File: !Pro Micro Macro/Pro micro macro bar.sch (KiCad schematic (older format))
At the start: 19 parts, among them U1 ProMicro

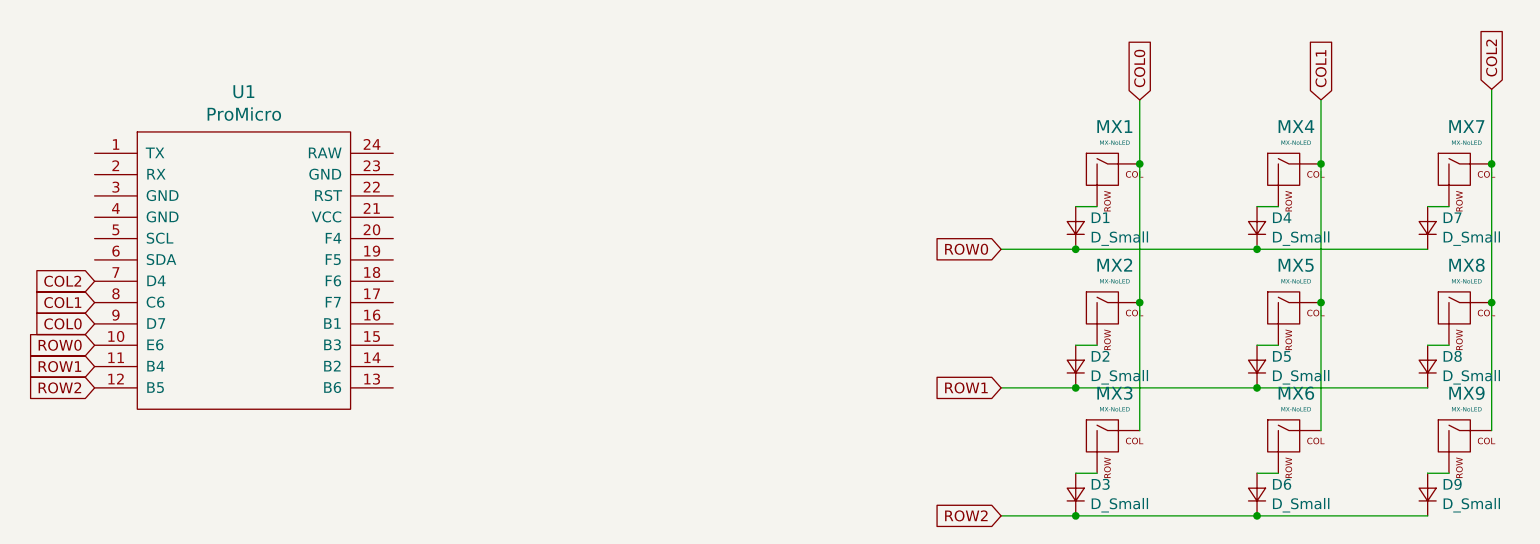
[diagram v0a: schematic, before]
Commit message: Redesigned pro micro
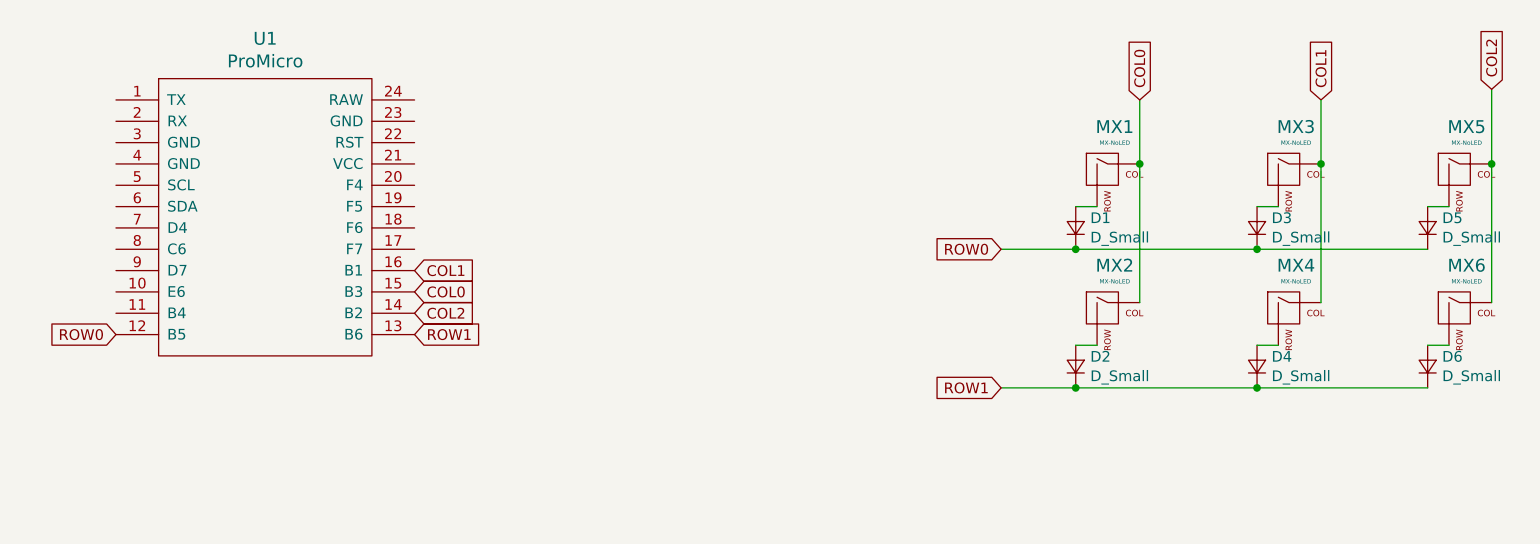
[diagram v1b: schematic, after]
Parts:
- removed D3, D6, D9: D_Small, Diode_THT:D_A-405_P10.16mm_Horizontal, symbol Device:D_Small
- removed MX3, MX6, MX9: MX-NoLED, Bases github:MX-1U-NoLED, symbol MX_Alps_Hybrid:MX-NoLED
- D1, D2: footprint Diode_THT:D_A-405_P10.16mm_Horizontal -> random-keyboard-parts:D_SOD-123-Pretty
- D3: renamed from D4; footprint Diode_THT:D_A-405_P10.16mm_Horizontal -> random-keyboard-parts:D_SOD-123-Pretty
- D4: renamed from D5; footprint Diode_THT:D_A-405_P10.16mm_Horizontal -> random-keyboard-parts:D_SOD-123-Pretty
- D5: renamed from D7; footprint Diode_THT:D_A-405_P10.16mm_Horizontal -> random-keyboard-parts:D_SOD-123-Pretty
- D6: renamed from D8; footprint Diode_THT:D_A-405_P10.16mm_Horizontal -> random-keyboard-parts:D_SOD-123-Pretty
- MX1, MX2: footprint Bases github:MX-1U-NoLED -> ! MX bases:MXOnly-1U-Hotswap
- MX3: renamed from MX4; footprint Bases github:MX-1U-NoLED -> ! MX bases:MXOnly-1U-Hotswap
- MX4: renamed from MX5; footprint Bases github:MX-1U-NoLED -> ! MX bases:MXOnly-1U-Hotswap
- MX5: renamed from MX7; footprint Bases github:MX-1U-NoLED -> ! MX bases:MXOnly-1U-Hotswap
- MX6: renamed from MX8; footprint Bases github:MX-1U-NoLED -> ! MX bases:MXOnly-1U-Hotswap
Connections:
- net ROW2 is gone; now on net ROW0: U1.12 (B5)
- net COL0: now also U1.15 (B3); no longer U1.9 (D7)
- net COL1: now also U1.16 (B1); no longer U1.8 (C6)
- net COL2: now also U1.14 (B2); no longer U1.7 (D4)
- net ROW0: no longer U1.10 (E6)
- net ROW1: now also U1.13 (B6); no longer U1.11 (B4)
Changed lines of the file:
@@
 $EndDescr
-$Comp
-L promicro:ProMicro U1
-U 1 1 5DA52A12
-P 3000 3350
-F 0 "U1" H 3000 4387 60  0000 C CNN
-F 1 "ProMicro" H 3000 4281 60  0000 C CNN
-F 2 "promicro:ProMicro" H 3100 2300 60  0001 C CNN
-F 3 "" H 3100 2300 60  0000 C CNN
-	1    3000 3350
-	1    0    0    -1
-$EndComp
 $Comp
 L MX_Alps_Hybrid:MX-NoLED MX1
@@
 F 0 "MX1" H 7083 2923 60  0000 C CNN
 F 1 "MX-NoLED" H 7083 2849 20  0000 C CNN
-F 2 "Bases github:MX-1U-NoLED" H 6425 2675 60  0001 C CNN
+F 2 "! MX bases:MXOnly-1U-Hotswap" H 6425 2675 60  0001 C CNN
 F 3 "" H 6425 2675 60  0001 C CNN
 	1    7050 2700
@@
 $EndComp
 $Comp
-L MX_Alps_Hybrid:MX-NoLED MX4
+L MX_Alps_Hybrid:MX-NoLED MX3
 U 1 1 5DA8BE76
 P 7900 2700
-F 0 "MX4" H 7933 2923 60  0000 C CNN
+F 0 "MX3" H 7933 2923 60  0000 C CNN
 F 1 "MX-NoLED" H 7933 2849 20  0000 C CNN
-F 2 "Bases github:MX-1U-NoLED" H 7275 2675 60  0001 C CNN
+F 2 "! MX bases:MXOnly-1U-Hotswap" H 7275 2675 60  0001 C CNN
 F 3 "" H 7275 2675 60  0001 C CNN
 	1    7900 2700
@@
 F 0 "MX2" H 7083 3573 60  0000 C CNN
 F 1 "MX-NoLED" H 7083 3499 20  0000 C CNN
-F 2 "Bases github:MX-1U-NoLED" H 6425 3325 60  0001 C CNN
+F 2 "! MX bases:MXOnly-1U-Hotswap" H 6425 3325 60  0001 C CNN
 F 3 "" H 6425 3325 60  0001 C CNN
 	1    7050 3350
@@
 $EndComp
 $Comp
-L MX_Alps_Hybrid:MX-NoLED MX5
+L MX_Alps_Hybrid:MX-NoLED MX4
 U 1 1 5DA8DC31
 P 7900 3350
-F 0 "MX5" H 7933 3573 60  0000 C CNN
+F 0 "MX4" H 7933 3573 60  0000 C CNN
 F 1 "MX-NoLED" H 7933 3499 20  0000 C CNN
-F 2 "Bases github:MX-1U-NoLED" H 7275 3325 60  0001 C CNN
+F 2 "! MX bases:MXOnly-1U-Hotswap" H 7275 3325 60  0001 C CNN
 F 3 "" H 7275 3325 60  0001 C CNN
 	1    7900 3350
@@
 $EndComp
 $Comp
-L MX_Alps_Hybrid:MX-NoLED MX3
-U 1 1 5DA8EA9F
-P 7050 3950
-F 0 "MX3" H 7083 4173 60  0000 C CNN
-F 1 "MX-NoLED" H 7083 4099 20  0000 C CNN
-F 2 "Bases github:MX-1U-NoLED" H 6425 3925 60  0001 C CNN
-F 3 "" H 6425 3925 60  0001 C CNN
-	1    7050 3950
-	1    0    0    -1
-$EndComp
-$Comp
 L MX_Alps_Hybrid:MX-NoLED MX6
-U 1 1 5DA8FABA
-P 7900 3950
-F 0 "MX6" H 7933 4173 60  0000 C CNN
-F 1 "MX-NoLED" H 7933 4099 20  0000 C CNN
-F 2 "Bases github:MX-1U-NoLED" H 7275 3925 60  0001 C CNN
-F 3 "" H 7275 3925 60  0001 C CNN
-	1    7900 3950
-	1    0    0    -1
-$EndComp
-$Comp
-L MX_Alps_Hybrid:MX-NoLED MX9
-U 1 1 5DA9020E
-P 8700 3950
-F 0 "MX9" H 8733 4173 60  0000 C CNN
-F 1 "MX-NoLED" H 8733 4099 20  0000 C CNN
-F 2 "Bases github:MX-1U-NoLED" H 8075 3925 60  0001 C CNN
-F 3 "" H 8075 3925 60  0001 C CNN
-	1    8700 3950
-	1    0    0    -1
-$EndComp
-$Comp
-L MX_Alps_Hybrid:MX-NoLED MX8
 U 1 1 5DA90606
 P 8700 3350
-F 0 "MX8" H 8733 3573 60  0000 C CNN
+F 0 "MX6" H 8733 3573 60  0000 C CNN
 F 1 "MX-NoLED" H 8733 3499 20  0000 C CNN
-F 2 "Bases github:MX-1U-NoLED" H 8075 3325 60  0001 C CNN
+F 2 "! MX bases:MXOnly-1U-Hotswap" H 8075 3325 60  0001 C CNN
 F 3 "" H 8075 3325 60  0001 C CNN
 	1    8700 3350
@@
 $EndComp
 $Comp
-L MX_Alps_Hybrid:MX-NoLED MX7
+L MX_Alps_Hybrid:MX-NoLED MX5
 U 1 1 5DA90C38
 P 8700 2700
-F 0 "MX7" H 8733 2923 60  0000 C CNN
+F 0 "MX5" H 8733 2923 60  0000 C CNN
 F 1 "MX-NoLED" H 8733 2849 20  0000 C CNN
-F 2 "Bases github:MX-1U-NoLED" H 8075 2675 60  0001 C CNN
+F 2 "! MX bases:MXOnly-1U-Hotswap" H 8075 2675 60  0001 C CNN
 F 3 "" H 8075 2675 60  0001 C CNN
 	1    8700 2700
@@
 	8050 2650 8050 3300
 Wire Wire Line
-	8050 3300 8050 3900
-Connection ~ 8050 3300
-Wire Wire Line
-	8850 3900 8850 3300
-Wire Wire Line
 	7200 2650 7200 3300
 Wire Wire Line
 	8850 3300 8850 2650
-Connection ~ 8850 3300
-Connection ~ 7200 3300
-Wire Wire Line
-	7200 3300 7200 3900
 Wire Wire Line
 	7200 2650 7200 2350
@@
 ROW1
 $Comp
-L Device:D_Small D4
+L Device:D_Small D3
 U 1 1 5DA9B93D
 P 7750 2950
-F 0 "D4" V 7796 2882 50  0000 R CNN
+F 0 "D3" V 7796 2882 50  0000 R CNN
 F 1 "D_Small" V 7705 2882 50  0000 R CNN
-F 2 "Diode_THT:D_A-405_P10.16mm_Horizontal" V 7750 2950 50  0001 C CNN
+F 2 "random-keyboard-parts:D_SOD-123-Pretty" V 7750 2950 50  0001 C CNN
 F 3 "~" V 7750 2950 50  0001 C CNN
 	1    7750 2950
@@
 $EndComp
 $Comp
-L Device:D_Small D7
+L Device:D_Small D5
 U 1 1 5DA9D77C
 P 8550 2950
-F 0 "D7" V 8596 2882 50  0000 R CNN
+F 0 "D5" V 8596 2882 50  0000 R CNN
 F 1 "D_Small" V 8505 2882 50  0000 R CNN
-F 2 "Diode_THT:D_A-405_P10.16mm_Horizontal" V 8550 2950 50  0001 C CNN
+F 2 "random-keyboard-parts:D_SOD-123-Pretty" V 8550 2950 50  0001 C CNN
 F 3 "~" V 8550 2950 50  0001 C CNN
 	1    8550 2950
@@
 $EndComp
 $Comp
-L Device:D_Small D8
+L Device:D_Small D6
 U 1 1 5DA9DF4D
 P 8550 3600
-F 0 "D8" V 8596 3532 50  0000 R CNN
+F 0 "D6" V 8596 3532 50  0000 R CNN
 F 1 "D_Small" V 8505 3532 50  0000 R CNN
-F 2 "Diode_THT:D_A-405_P10.16mm_Horizontal" V 8550 3600 50  0001 C CNN
+F 2 "random-keyboard-parts:D_SOD-123-Pretty" V 8550 3600 50  0001 C CNN
 F 3 "~" V 8550 3600 50  0001 C CNN
 	1    8550 3600
@@
 $EndComp
 $Comp
-L Device:D_Small D9
-U 1 1 5DA9E796
-P 8550 4200
-F 0 "D9" V 8596 4132 50  0000 R CNN
-F 1 "D_Small" V 8505 4132 50  0000 R CNN
-F 2 "Diode_THT:D_A-405_P10.16mm_Horizontal" V 8550 4200 50  0001 C CNN
-F 3 "~" V 8550 4200 50  0001 C CNN
-	1    8550 4200
-	0    -1   -1   0
-$EndComp
-$Comp
-L Device:D_Small D5
+L Device:D_Small D4
 U 1 1 5DA9EF35
 P 7750 3600
-F 0 "D5" V 7796 3532 50  0000 R CNN
+F 0 "D4" V 7796 3532 50  0000 R CNN
 F 1 "D_Small" V 7705 3532 50  0000 R CNN
-F 2 "Diode_THT:D_A-405_P10.16mm_Horizontal" V 7750 3600 50  0001 C CNN
+F 2 "random-keyboard-parts:D_SOD-123-Pretty" V 7750 3600 50  0001 C CNN
 F 3 "~" V 7750 3600 50  0001 C CNN
 	1    7750 3600
@@
 F 0 "D2" V 6946 3532 50  0000 R CNN
 F 1 "D_Small" V 6855 3532 50  0000 R CNN
-F 2 "Diode_THT:D_A-405_P10.16mm_Horizontal" V 6900 3600 50  0001 C CNN
+F 2 "random-keyboard-parts:D_SOD-123-Pretty" V 6900 3600 50  0001 C CNN
 F 3 "~" V 6900 3600 50  0001 C CNN
 	1    6900 3600
-	0    -1   -1   0
-$EndComp
-$Comp
-L Device:D_Small D3
-U 1 1 5DA9FEF5
-P 6900 4200
-F 0 "D3" V 6946 4132 50  0000 R CNN
-F 1 "D_Small" V 6855 4132 50  0000 R CNN
-F 2 "Diode_THT:D_A-405_P10.16mm_Horizontal" V 6900 4200 50  0001 C CNN
-F 3 "~" V 6900 4200 50  0001 C CNN
-	1    6900 4200
 	0    -1   -1   0
 $EndComp
@@
 F 0 "D1" V 6946 2882 50  0000 R CNN
 F 1 "D_Small" V 6855 2882 50  0000 R CNN
-F 2 "Diode_THT:D_A-405_P10.16mm_Horizontal" V 6900 2950 50  0001 C CNN
+F 2 "random-keyboard-parts:D_SOD-123-Pretty" V 6900 2950 50  0001 C CNN
 F 3 "~" V 6900 2950 50  0001 C CNN
 	1    6900 2950
 	0    -1   -1   0
 $EndComp
-$Comp
-L Device:D_Small D6
-U 1 1 5DAA17A9
-P 7750 4200
-F 0 "D6" V 7796 4132 50  0000 R CNN
-F 1 "D_Small" V 7705 4132 50  0000 R CNN
-F 2 "Diode_THT:D_A-405_P10.16mm_Horizontal" V 7750 4200 50  0001 C CNN
-F 3 "~" V 7750 4200 50  0001 C CNN
-	1    7750 4200
-	0    -1   -1   0
-$EndComp
 Wire Wire Line
 	6900 2850 7000 2850
@@
 	8550 3500 8650 3500
 Wire Wire Line
-	8550 4100 8650 4100
-Wire Wire Line
-	7750 4100 7850 4100
-Wire Wire Line
 	7750 3500 7850 3500
 Wire Wire Line
 	6900 3500 7000 3500
-Wire Wire Line
-	6900 4100 7000 4100
-Wire Wire Line
-	8550 4300 7750 4300
-Wire Wire Line
-	7750 4300 6900 4300
-Connection ~ 7750 4300
-Wire Wire Line
-	6900 4300 6550 4300
-Connection ~ 6900 4300
 Wire Wire Line
 	8550 3700 7750 3700
@@
 	6900 3050 6550 3050
 Connection ~ 6900 3050
-Text GLabel 6550 4300 0    50   Input ~ 0
-ROW2
 Text GLabel 7200 2350 1    50   Input ~ 0
 COL0
@@
 Text GLabel 8850 2300 1    50   Input ~ 0
 COL2
-Text GLabel 2300 3700 0    50   Input ~ 0
-ROW2
-Text GLabel 2300 3600 0    50   Input ~ 0
+$Comp
+L promicro:ProMicro U1
+U 1 1 5DCF2F33
+P 3100 3100
+F 0 "U1" H 3100 4137 60  0000 C CNN
+F 1 "ProMicro" H 3100 4031 60  0000 C CNN
+F 2 "promicro:ProMicro" H 3200 2050 60  0001 C CNN
+F 3 "" H 3200 2050 60  0000 C CNN
+	1    3100 3100
+	1    0    0    -1
+$EndComp
+Text GLabel 2400 3450 0    50   Input ~ 0
+ROW0
+Text GLabel 3800 3450 2    50   Input ~ 0
 ROW1
-Text GLabel 2300 3500 0    50   Input ~ 0
-ROW0
-Text GLabel 2300 3400 0    50   Input ~ 0
+Text GLabel 3800 3250 2    50   Input ~ 0
 COL0
-Text GLabel 2300 3300 0    50   Input ~ 0
+Text GLabel 3800 3350 2    50   Input ~ 0
+COL2
+Text GLabel 3800 3150 2    50   Input ~ 0
 COL1
-Text GLabel 2300 3200 0    50   Input ~ 0
-COL2
 $EndSCHEMATC
